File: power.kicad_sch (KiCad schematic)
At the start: 43 parts, among them P10 PH_A, P11 SUPPLY, P12 GND, P8 PH_C, P9 PH_B, Q1 STL130N6F7, Q2 STL130N6F7, Q3 STL130N6F7, Q4 STL130N6F7, Q5 STL130N6F7, Q6 STL130N6F7, U5 AD8418, U6 AD8418, U7 AD8418

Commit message: started power stage
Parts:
- P10, P11, P12, P8, P9: footprint (none) -> Connector_Pin:Pin_D1.0mm_L10.0mm_LooseFit
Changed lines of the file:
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@@
 			)
 		)
-		(property "Footprint" ""
+		(property "Footprint" "Connector_Pin:Pin_D1.0mm_L10.0mm_LooseFit"
 			(at 19.05 55.88 0)
 			(effects
@@
 			)
 		)
-		(property "Footprint" ""
+		(property "Footprint" "Connector_Pin:Pin_D1.0mm_L10.0mm_LooseFit"
 			(at 113.03 54.61 0)
 			(effects
@@
 			)
 		)
-		(property "Footprint" ""
+		(property "Footprint" "Connector_Pin:Pin_D1.0mm_L10.0mm_LooseFit"
 			(at 200.66 55.88 0)
 			(effects
@@
 			)
 		)
-		(property "Footprint" ""
+		(property "Footprint" "Connector_Pin:Pin_D1.0mm_L10.0mm_LooseFit"
 			(at 262.89 27.94 0)
 			(effects
@@
 			)
 		)
-		(property "Footprint" ""
+		(property "Footprint" "Connector_Pin:Pin_D1.0mm_L10.0mm_LooseFit"
 			(at 271.78 107.95 0)
 			(effects

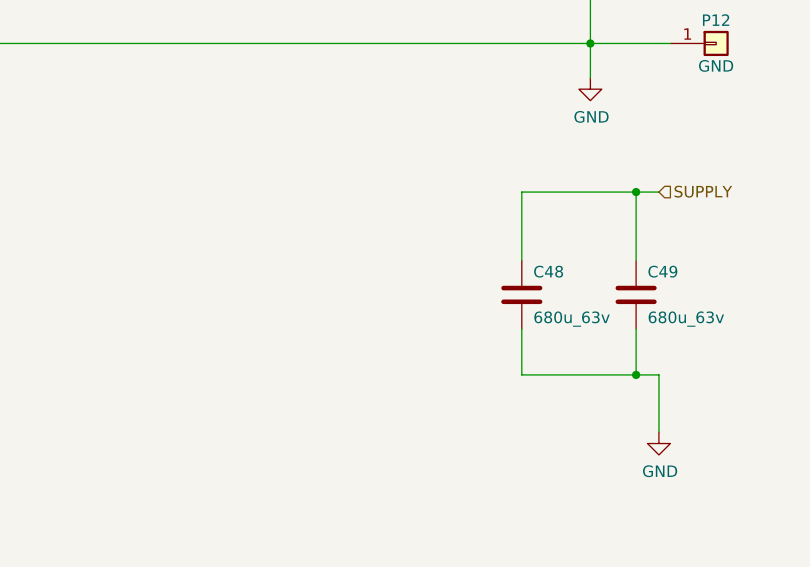
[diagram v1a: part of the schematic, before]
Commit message: more routing connectors and caps
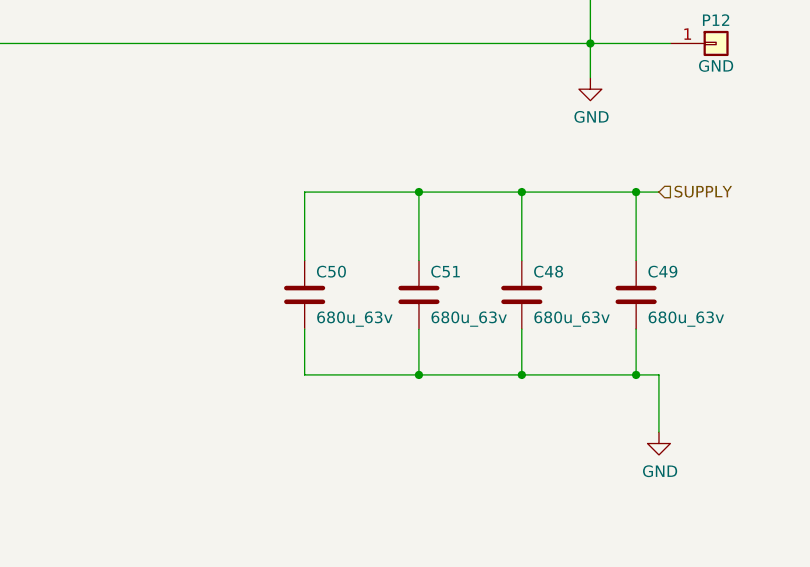
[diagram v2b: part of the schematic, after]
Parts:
- added C50, C51: 680u_63v, Capacitor_SMD:CP_Elec_10x10.5, symbol Device:C
- C48, C49: footprint (none) -> Capacitor_SMD:CP_Elec_10x10.5
- P10, P8, P9: footprint Connector_Pin:Pin_D1.0mm_L10.0mm_LooseFit -> Connector_Pin:Pin_D1.3mm_L11.0mm_LooseFit
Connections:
- net GND: now also C50.2, C51.2
- net SUPPLY: now also C50.1, C51.1
